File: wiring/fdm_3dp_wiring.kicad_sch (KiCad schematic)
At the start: 9 parts, among them K1 SANYOU_SRD_Form_C, M1 Stepper_Motor_bipolar, U2 TB6600, U3 JTD1548D05

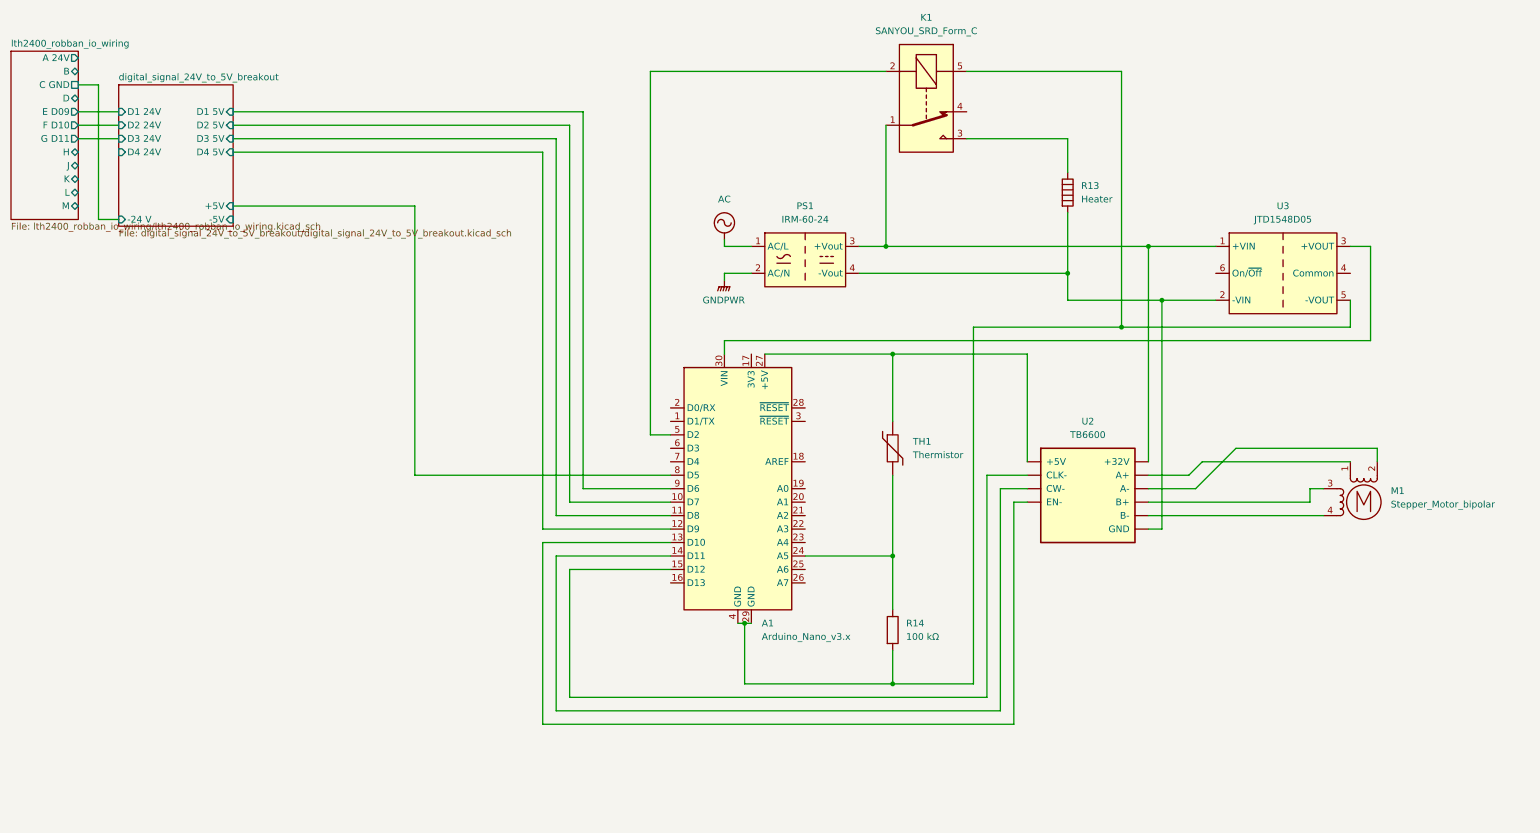
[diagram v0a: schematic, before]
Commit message: update schematic to reflect new thermistor breakout
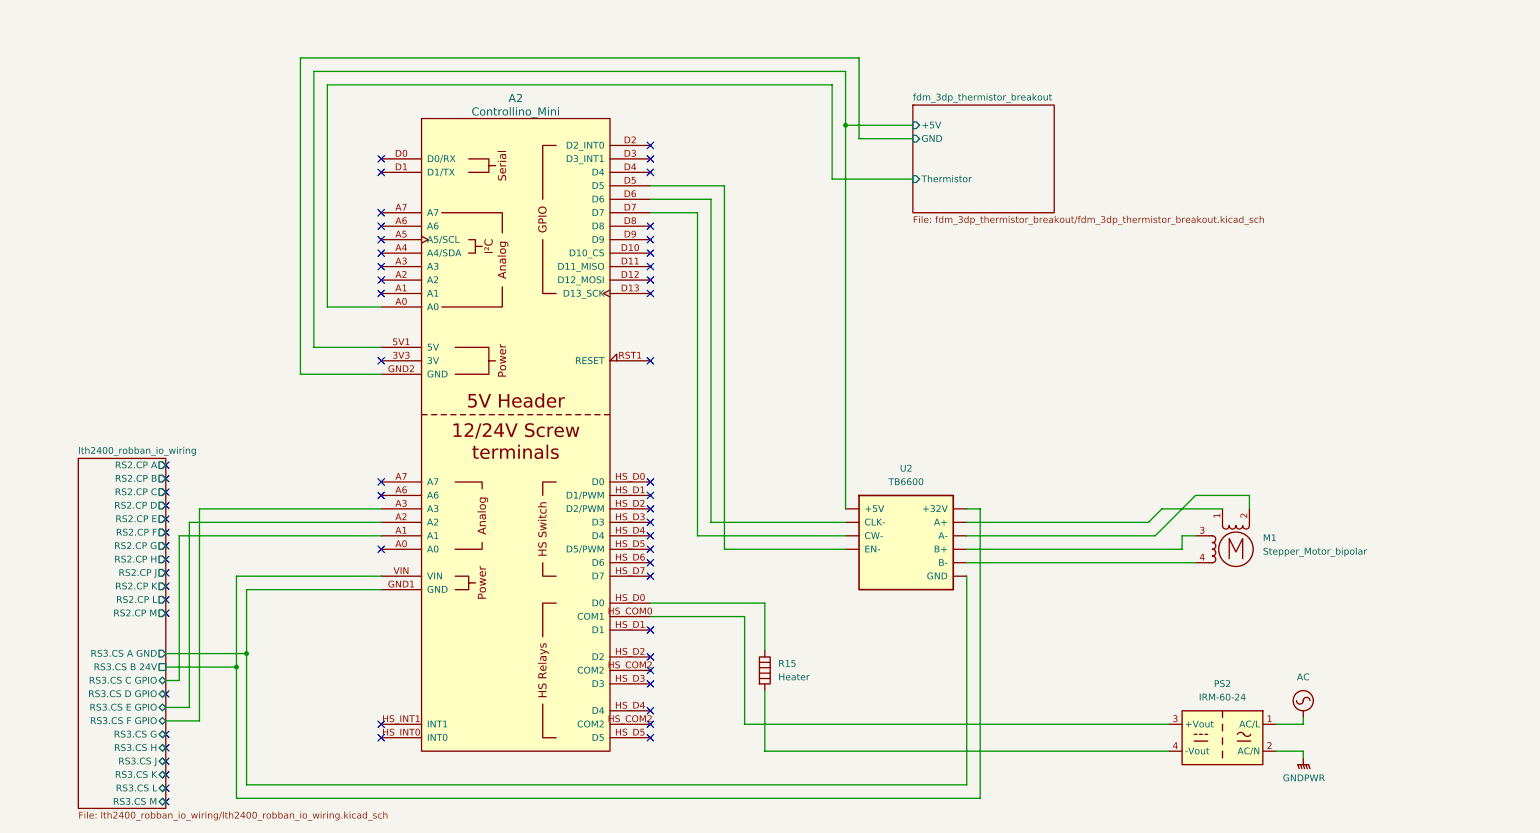
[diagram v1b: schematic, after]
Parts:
- removed A1: Arduino_Nano_v3.x, Module:Arduino_Nano, symbol MCU_Module:Arduino_Nano_v3.x
- removed K1: SANYOU_SRD_Form_C, Relay_THT:Relay_SPDT_SANYOU_SRD_Series_Form_C, symbol Relay:SANYOU_SRD_Form_C
- removed PS1: IRM-60-24, Converter_ACDC:Converter_ACDC_MeanWell_IRM-60-xx_THT, symbol Converter_ACDC:IRM-60-24
- removed R13: Heater, symbol Device:Heater
- removed R14: 100 kΩ, symbol Device:R
- removed TH1: Thermistor, symbol Device:Thermistor
- removed U3: JTD1548D05, Converter_DCDC:Converter_DCDC_XP_POWER_JTDxxxxxxx_THT, symbol Converter_DCDC:JTD1548D05
- added A2: Controllino_Mini, symbol fdm_3dp_wiring:Controllino_Mini
- added PS2: IRM-60-24, Converter_ACDC:Converter_ACDC_MeanWell_IRM-60-xx_THT, symbol Converter_ACDC:IRM-60-24
- added R15: Heater, symbol Device:Heater
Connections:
- net AC: now also PS2.1 (AC/L)
- net GNDPWR: now also PS2.2 (AC/N)
- net lth2400_robban_io_wiring/RS3.CS B 24V: now reaches U2.~ (GND)
- net lth2400_robban_io_wiring/RS3.CS B 24V: now also A2.VIN
- new net: A2.D5, U2.~ (GND)
- new net: A2.D6, U2.~ (GND)
- new net: A2.D7, U2.~ (GND)
- new net: A2.HS_COM0 (COM1), PS2.3 (+Vout)
- new net: A2.HS_D0 (D0), R15.1
- new net: PS2.4 (-Vout), R15.2
- new net fdm_3dp_thermistor_breakout/+5V: A2.5V1 (5V), U2.~ (GND)
- new net fdm_3dp_thermistor_breakout/GND: A2.GND2 (GND)
- new net fdm_3dp_thermistor_breakout/Thermistor: A2.A0
- new net lth2400_robban_io_wiring/RS3.CS A GND: A2.GND1 (GND), U2.~ (GND)
- new net lth2400_robban_io_wiring/RS3.CS C GPIO: A2.A1
- new net lth2400_robban_io_wiring/RS3.CS E GPIO: A2.A2
- new net lth2400_robban_io_wiring/RS3.CS F GPIO: A2.A3
- no-connect marks 0 -> 59
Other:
- removed sheet digital_signal_24V_to_5V_breakout
- added sheet fdm_3dp_thermistor_breakout (fdm_3dp_thermistor_breakout/fdm_3dp_thermistor_breakout.kicad_sch)
- sheet lth2400_robban_io_wiring ports: added RS2.CP A, RS2.CP B, RS2.CP C, RS2.CP D, RS2.CP E, RS2.CP F, RS2.CP G, RS2.CP H, RS2.CP J, RS2.CP K, RS2.CP L, RS2.CP M, RS3.CS A GND, RS3.CS B 24V, RS3.CS C GPIO, RS3.CS D GPIO, RS3.CS E GPIO, RS3.CS F GPIO, RS3.CS G, RS3.CS H, RS3.CS J, RS3.CS K, RS3.CS L, RS3.CS M; removed A 24V, B, C GND, D, E D09, F D10, G D11, H, J, K, L, M
- moved on the sheet: M1, U2
